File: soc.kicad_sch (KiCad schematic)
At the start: 70 parts, among them U1 MPFS250T-FCVG484

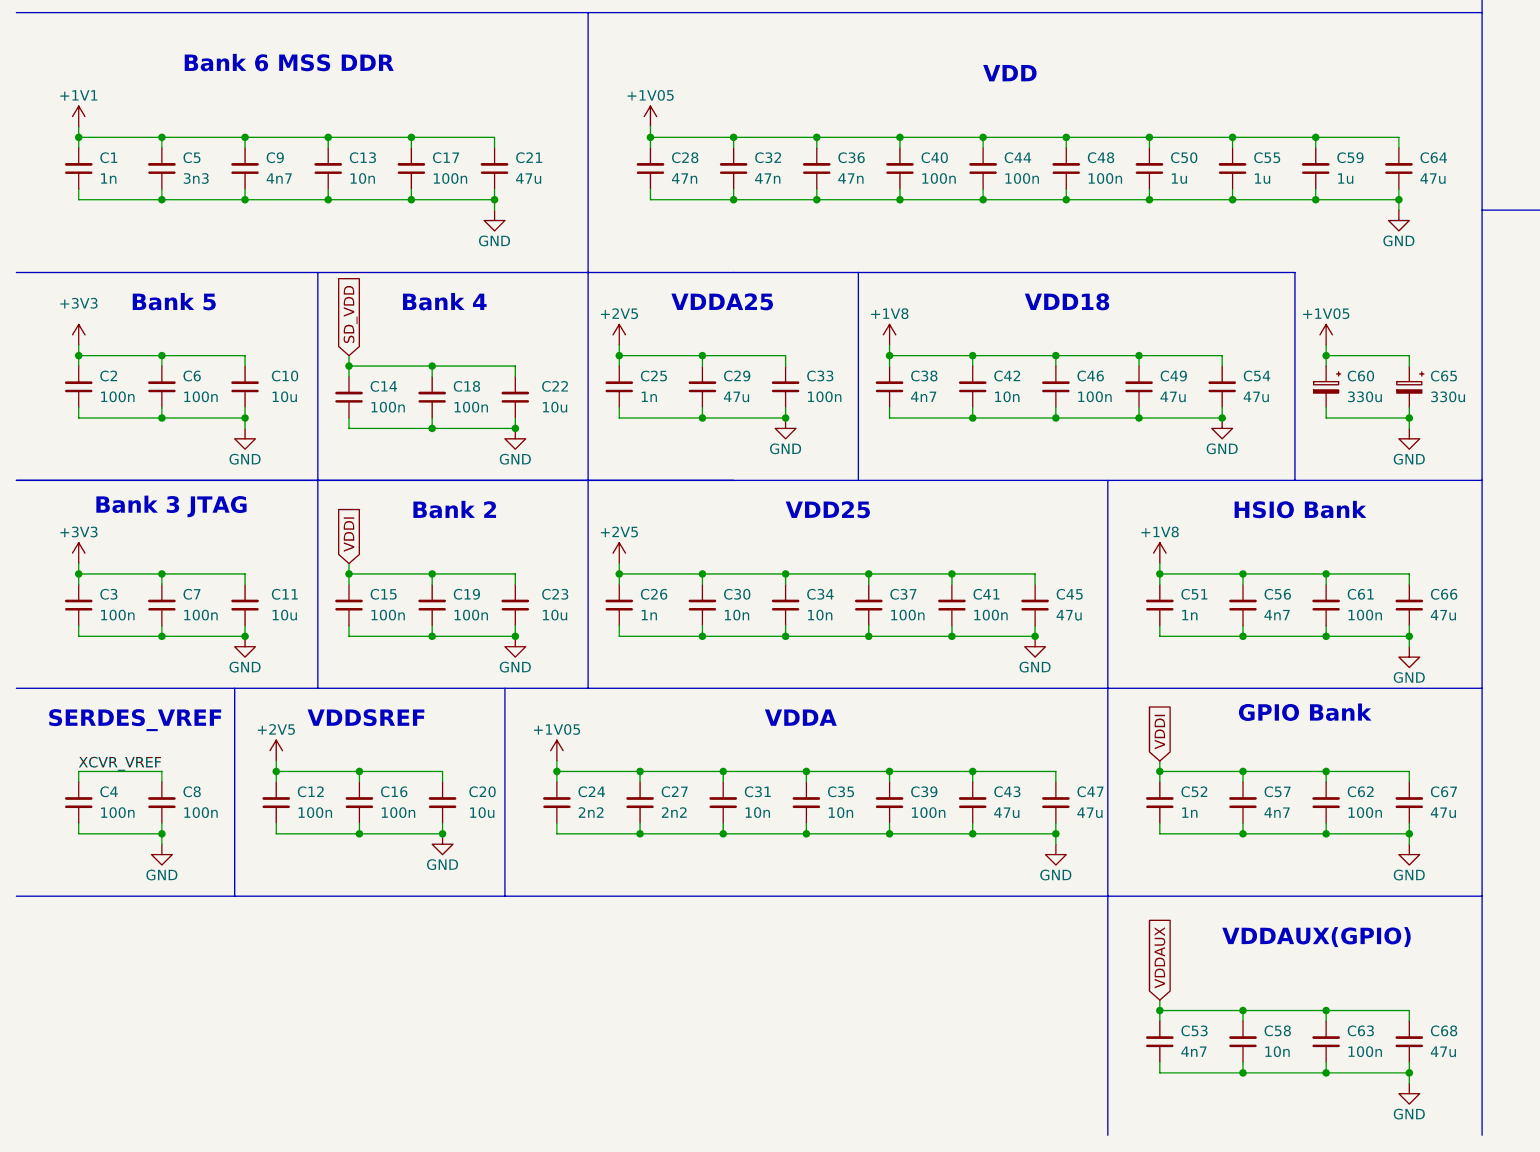
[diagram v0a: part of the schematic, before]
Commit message: [#55992] Replace 100n capacitors
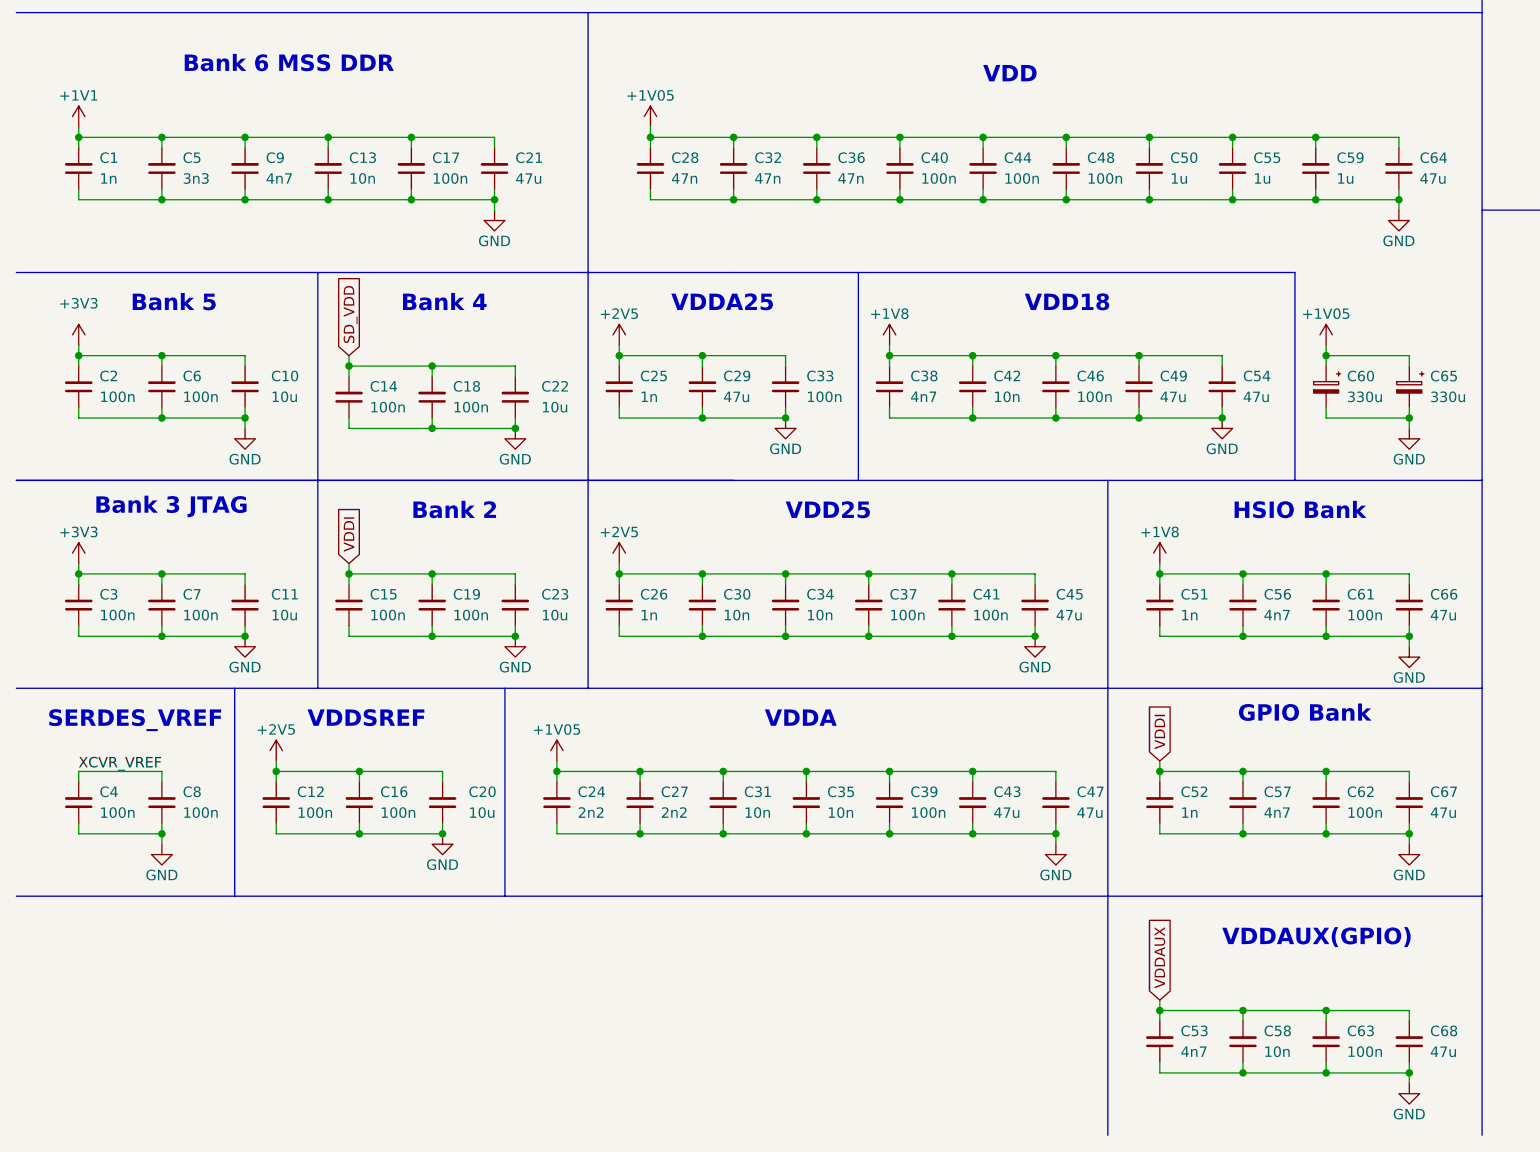
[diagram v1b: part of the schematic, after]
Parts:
- C1, C25, C26, C51, C52: value C_1n_0201 -> C_1n_0402; footprint antmicro-footprints:C_0201 -> antmicro-footprints:C_0402_1005Metric; symbol antmicroCapacitorsmisc:C_1n_0201 -> antmicroCapacitors0402:C_1n_0402; Dielectric X7R -> C0G; MPN GRM033R71H102KA12D -> GRM1555C1H102JA01D
- C12, C14, C15, C16, C17, C18, C19, C2, C3, C33, C37, C39, C4, C40, C41, C44, C46, C48, C6, C61, C62, C63, C7, C8: value C_100n_0201_25V -> C_100n_0402; footprint antmicro-footprints:C_0201 -> antmicro-footprints:C_0402_1005Metric; symbol antmicroCapacitorsmisc:C_100n_0201_25V -> antmicroCapacitors0402:C_100n_0402; MPN C0603X5R1E104K030BB -> GRM155R61H104KE14D; Manufacturer TDK -> Murata; Voltage 25V -> 50V
- C13, C30, C31, C34, C35, C42, C58: value C_10n_0201 -> C_10n_0402; footprint antmicro-footprints:C_0201 -> antmicro-footprints:C_0402_1005Metric; symbol antmicroCapacitorsmisc:C_10n_0201 -> antmicroCapacitors0402:C_10n_0402; Dielectric X5R -> X7R; MPN GRM033R61E103KA12D -> GRM155R71H103KA88D; Voltage 25V -> 50V
- C24, C27: value C_2n2_0201 -> C_2n2_0402; footprint antmicro-footprints:C_0201 -> antmicro-footprints:C_0402_1005Metric; symbol antmicroCapacitorsmisc:C_2n2_0201 -> antmicroCapacitors0402:C_2n2_0402; MPN GRM033R71E222KA12D -> C0402C222J5RACTU; Manufacturer Murata -> KEMET
- C28, C32, C36: value C_47n_0201 -> C_47n_0402; footprint antmicro-footprints:C_0201 -> antmicro-footprints:C_0402_1005Metric; symbol antmicroCapacitorsmisc:C_47n_0201 -> antmicroCapacitors0402:C_47n_0402; MPN GRM033R61A473KE84D -> GRM155R61H474KE11D
- C38, C53, C56, C57, C9: value C_4n7_0201 -> C_4n7_0402; footprint antmicro-footprints:C_0201 -> antmicro-footprints:C_0402_1005Metric; symbol antmicroCapacitorsmisc:C_4n7_0201 -> antmicroCapacitors0402:C_4n7_0402; MPN GRM033R71E472KE14D -> CGA2B3X7S2A472K050BB; Manufacturer Murata -> TDK
- C5: value C_3n3_0201 -> C_3n3_0402; footprint antmicro-footprints:C_0201 -> antmicro-footprints:C_0402_1005Metric; symbol antmicroCapacitorsmisc:C_3n3_0201 -> antmicroCapacitors0402:C_3n3_0402; MPN GRM033R71E332KA12D -> C0402C332K5RAC; Manufacturer Murata -> KEMET; Voltage 25V -> 50V
- C50, C55, C59: value C_1u_0201 -> C_1u_0402; footprint antmicro-footprints:C_0201 -> antmicro-footprints:C_0402_1005Metric; symbol antmicroCapacitorsmisc:C_1u_0201_16V -> antmicroCapacitors0402:C_1u_0402; MPN GRM033R61C105ME15D -> C1005X6S1A105K050BC; Manufacturer Murata -> TDK

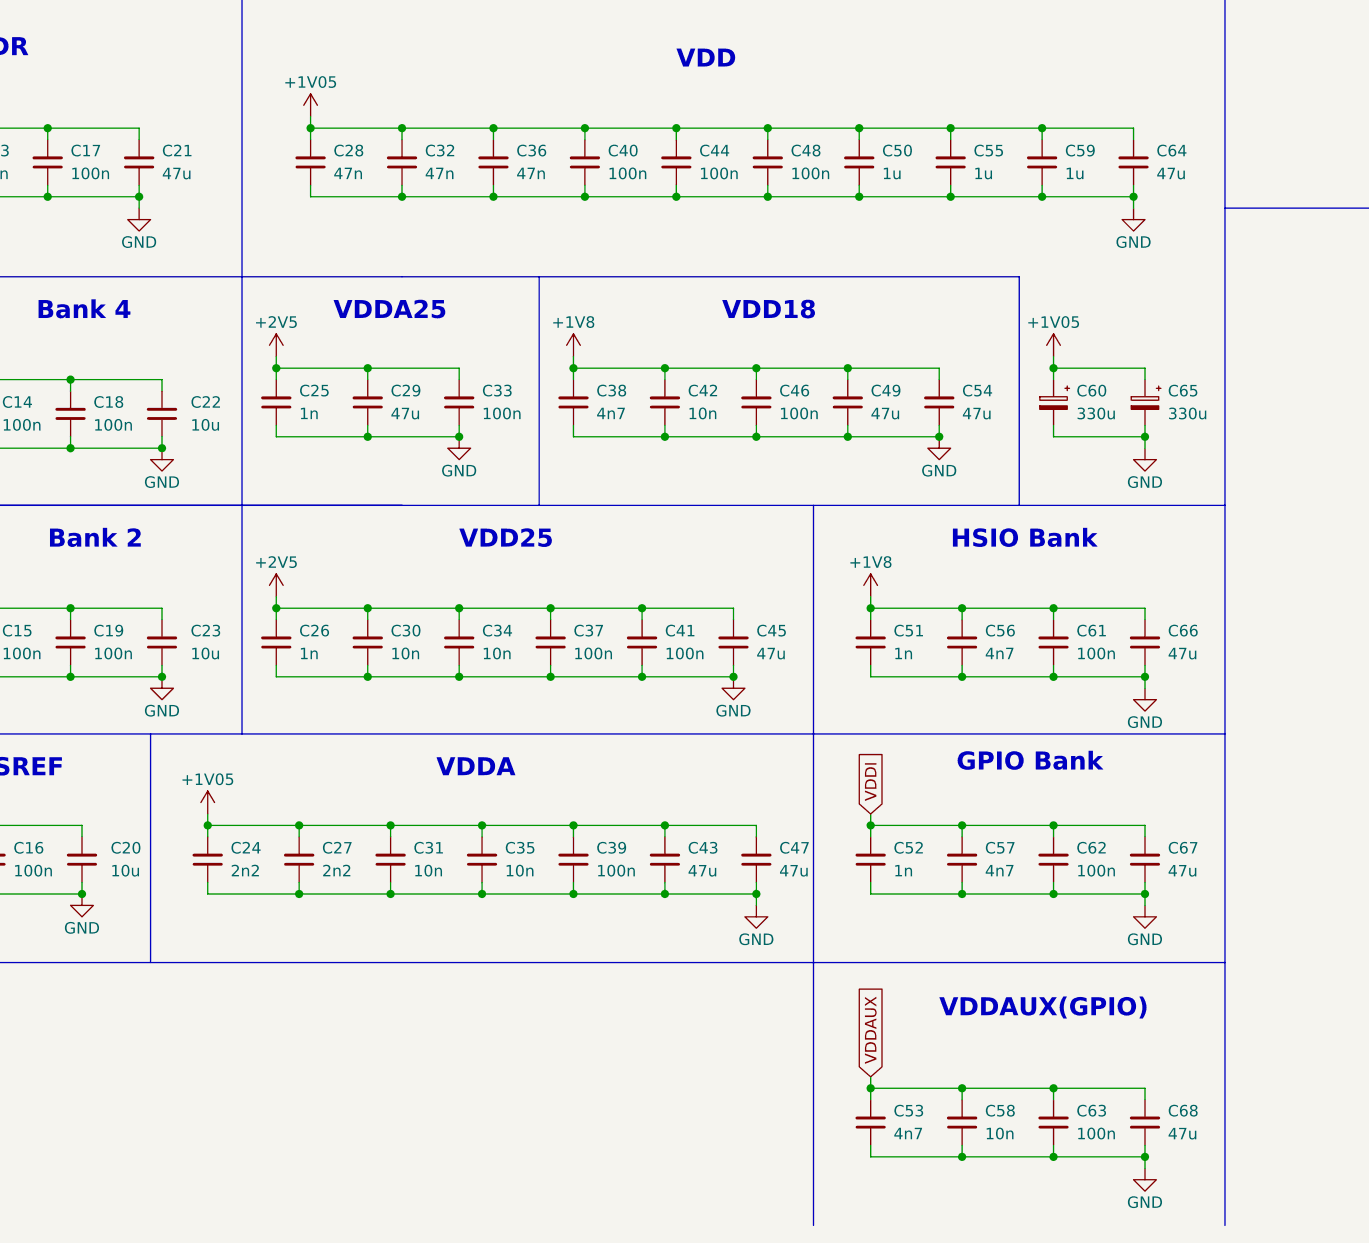
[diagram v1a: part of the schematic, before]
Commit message: [#56060] Place decoupling under FPGA
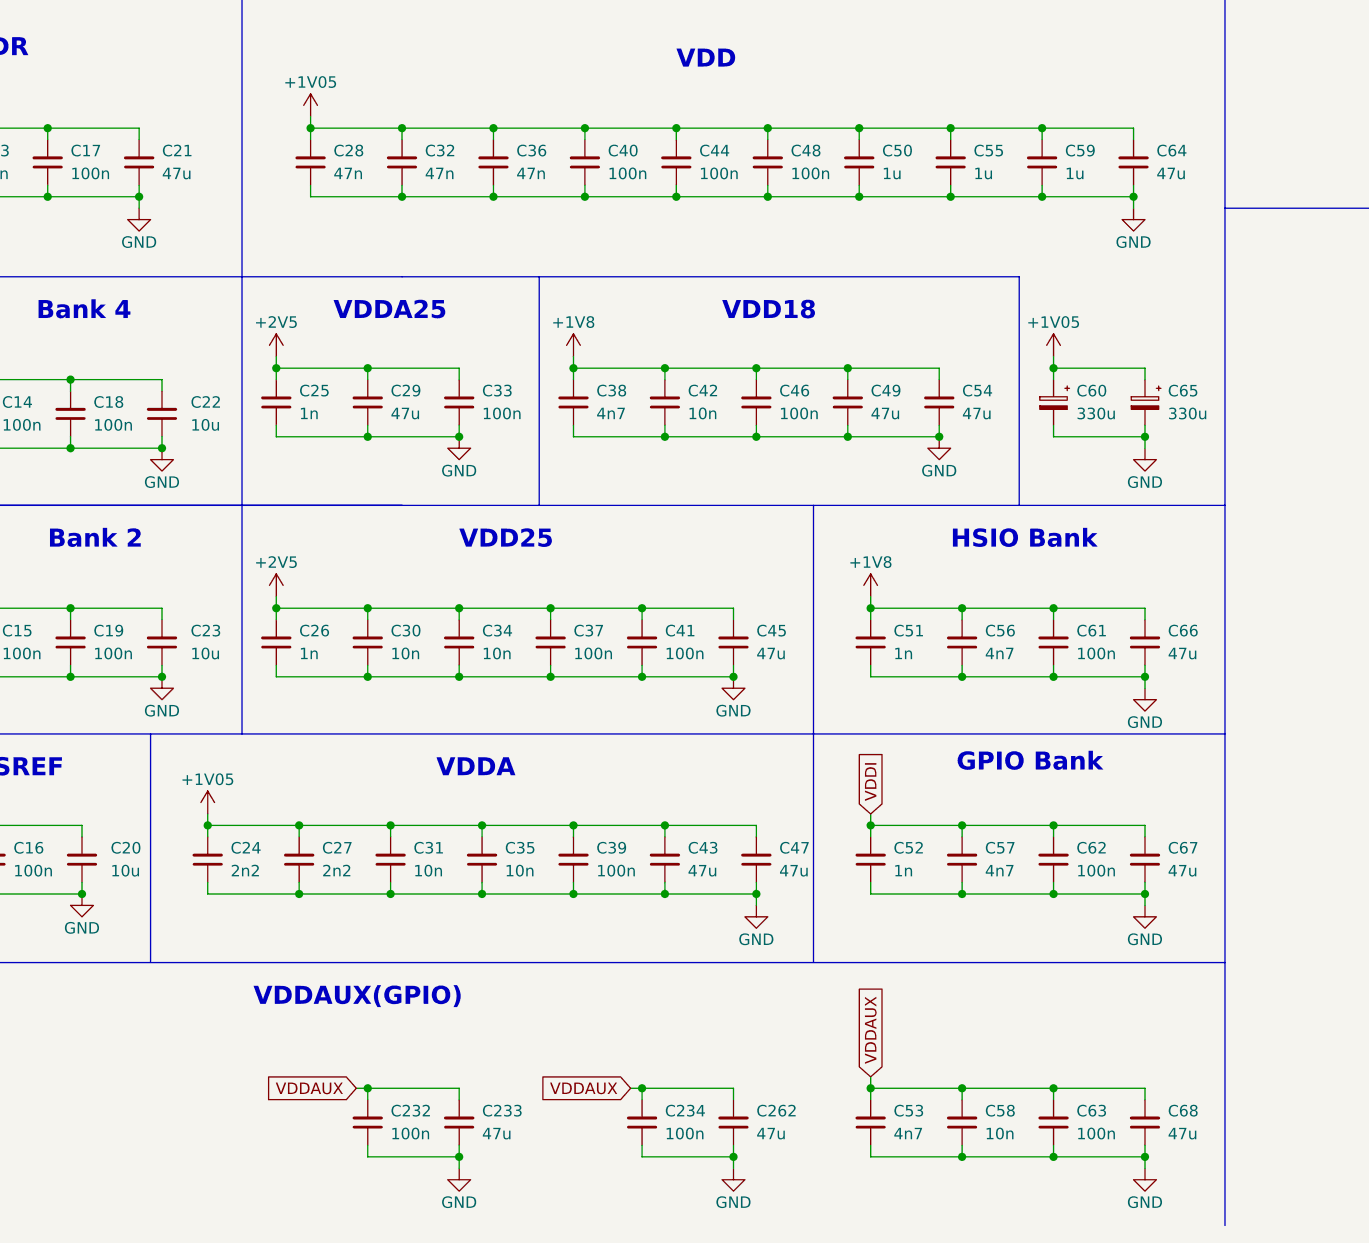
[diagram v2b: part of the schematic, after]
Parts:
- added C232, C234: C_100n_0402, antmicro-footprints:C_0402_1005Metric, symbol antmicroCapacitors0402:C_100n_0402
- added C233, C262: C_47u_0603, antmicro-footprints:C_0603_1608Metric, symbol antmicroCapacitors0603:C_47u_0603
- C21, C29, C43, C45, C47, C49, C54, C64, C66, C67, C68: value C_47u_0402_50V_X7R -> C_47u_0603; footprint antmicro-footprints:C_0402_1005Metric -> antmicro-footprints:C_0603_1608Metric; symbol antmicroCapacitors0402:C_47u_0402_50V_X7R -> antmicroCapacitors0603:C_47u_0603; MPN KRM55WR71H476MH13L -> GRM188R60J476ME15D; Val 47u/50V/X7R -> 47u
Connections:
- net GND: now also C232.1, C233.1, C234.1, C262.1
- net VDDAUX: now also C232.2, C233.2, C234.2, C262.2
